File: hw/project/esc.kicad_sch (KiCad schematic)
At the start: 0 parts

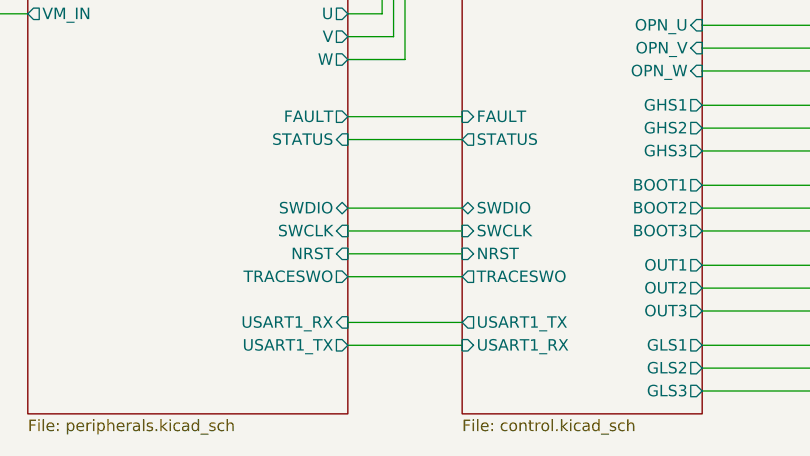
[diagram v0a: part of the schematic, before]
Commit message: Revise hall sensor inputs
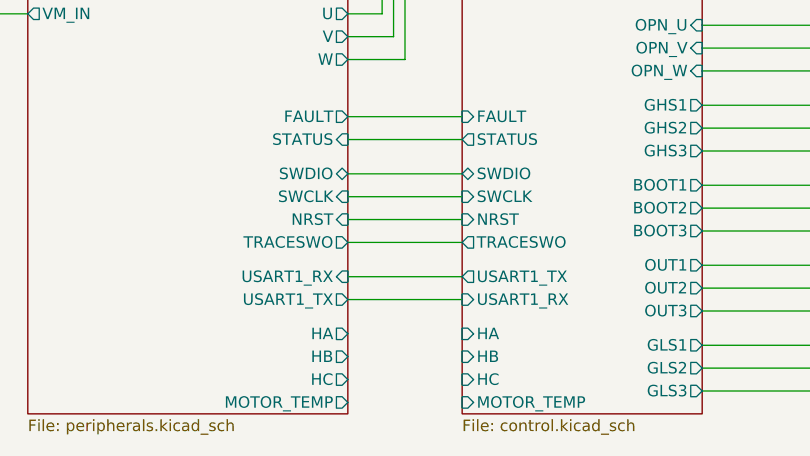
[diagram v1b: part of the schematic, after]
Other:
- sheet Control ports: added HA, HB, HC, MOTOR_TEMP; removed none
- sheet Peripherals ports: added HA, HB, HC, MOTOR_TEMP; removed none
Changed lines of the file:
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@@
 	(wire
 		(pts
-			(xy 165.1 123.19) (xy 152.4 123.19)
-		)
-		(stroke
-			(width 0)
-			(type default)
-		)
-	)
-	(wire
-		(pts
-			(xy 165.1 113.03) (xy 152.4 113.03)
+			(xy 165.1 118.11) (xy 152.4 118.11)
+		)
+		(stroke
+			(width 0)
+			(type default)
+		)
+	)
+	(wire
+		(pts
+			(xy 165.1 109.22) (xy 152.4 109.22)
 		)
 		(stroke
@@
 	(wire
 		(pts
-			(xy 165.1 107.95) (xy 152.4 107.95)
+			(xy 165.1 104.14) (xy 152.4 104.14)
 		)
 		(stroke
@@
 	(wire
 		(pts
-			(xy 165.1 120.65) (xy 152.4 120.65)
+			(xy 165.1 115.57) (xy 152.4 115.57)
 		)
 		(stroke
@@
 	(wire
 		(pts
-			(xy 165.1 110.49) (xy 152.4 110.49)
+			(xy 165.1 106.68) (xy 152.4 106.68)
 		)
 		(stroke
@@
 	(wire
 		(pts
-			(xy 165.1 115.57) (xy 152.4 115.57)
+			(xy 165.1 111.76) (xy 152.4 111.76)
 		)
 		(stroke
@@
 		)
 		(pin "NRST" input
-			(at 165.1 113.03 180)
+			(at 165.1 109.22 180)
 			(effects
 				(font
@@
 		)
 		(pin "SWCLK" input
-			(at 165.1 110.49 180)
+			(at 165.1 106.68 180)
 			(effects
 				(font
@@
 		)
 		(pin "TRACESWO" output
-			(at 165.1 115.57 180)
+			(at 165.1 111.76 180)
 			(effects
 				(font
@@
 		)
 		(pin "SWDIO" bidirectional
-			(at 165.1 107.95 180)
+			(at 165.1 104.14 180)
 			(effects
 				(font
@@
 		)
 		(pin "USART1_TX" output
-			(at 165.1 120.65 180)
+			(at 165.1 115.57 180)
 			(effects
 				(font
@@
 		)
 		(pin "USART1_RX" input
-			(at 165.1 123.19 180)
+			(at 165.1 118.11 180)
 			(effects
 				(font
@@
 		(pin "STATUS" output
 			(at 165.1 100.33 180)
+			(effects
+				(font
+					(size 1.27 1.27)
+				)
+				(justify left)
+			)
+		)
+		(pin "HA" input
+			(at 165.1 121.92 180)
+			(effects
+				(font
+					(size 1.27 1.27)
+				)
+				(justify left)
+			)
+		)
+		(pin "HB" input
+			(at 165.1 124.46 180)
+			(effects
+				(font
+					(size 1.27 1.27)
+				)
+				(justify left)
+			)
+		)
+		(pin "HC" input
+			(at 165.1 127 180)
+			(effects
+				(font
+					(size 1.27 1.27)
+				)
+				(justify left)
+			)
+		)
+		(pin "MOTOR_TEMP" input
+			(at 165.1 129.54 180)
 			(effects
 				(font
@@
 		)
 		(pin "NRST" input
-			(at 152.4 113.03 0)
+			(at 152.4 109.22 0)
 			(effects
 				(font
@@
 		)
 		(pin "SWCLK" input
-			(at 152.4 110.49 0)
+			(at 152.4 106.68 0)
 			(effects
 				(font
@@
 		)
 		(pin "SWDIO" bidirectional
-			(at 152.4 107.95 0)
+			(at 152.4 104.14 0)
 			(effects
 				(font
@@
 		)
 		(pin "TRACESWO" output
-			(at 152.4 115.57 0)
+			(at 152.4 111.76 0)
 			(effects
 				(font
@@
 		)
 		(pin "USART1_RX" input
-			(at 152.4 120.65 0)
+			(at 152.4 115.57 0)
 			(effects
 				(font
@@
 		)
 		(pin "USART1_TX" output
-			(at 152.4 123.19 0)
+			(at 152.4 118.11 0)
 			(effects
 				(font
@@
 			)
 		)
+		(pin "HA" output
+			(at 152.4 121.92 0)
+			(effects
+				(font
+					(size 1.27 1.27)
+				)
+				(justify right)
+			)
+		)
+		(pin "HB" output
+			(at 152.4 124.46 0)
+			(effects
+				(font
+					(size 1.27 1.27)
+				)
+				(justify right)
+			)
+		)
+		(pin "HC" output
+			(at 152.4 127 0)
+			(effects
+				(font
+					(size 1.27 1.27)
+				)
+				(justify right)
+			)
+		)
+		(pin "MOTOR_TEMP" output
+			(at 152.4 129.54 0)
+			(effects
+				(font
+					(size 1.27 1.27)
+				)
+				(justify right)
+			)
+		)

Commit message: can tranceiver
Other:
- sheet Control ports: added CAN_STBY, FDCAN1_RX, FDCAN1_TX; removed none
- sheet Peripherals ports: added RXD, STBY, TXD; removed none
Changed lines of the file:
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@@
+	(wire
+		(pts
+			(xy 152.4 140.97) (xy 165.1 140.97)
+		)
+		(stroke
+			(width 0)
+			(type default)
+		)
+	)
 	(wire
 		(pts
@@
 	(wire
 		(pts
+			(xy 152.4 146.05) (xy 165.1 146.05)
+		)
+		(stroke
+			(width 0)
+			(type default)
+		)
+	)
+	(wire
+		(pts
 			(xy 157.48 88.9) (xy 152.4 88.9)
 		)
@@
 		(pts
 			(xy 156.21 69.85) (xy 156.21 86.36)
+		)
+		(stroke
+			(width 0)
+			(type default)
+		)
+	)
+	(wire
+		(pts
+			(xy 152.4 143.51) (xy 165.1 143.51)
 		)
 		(stroke
@@
 	(sheet
 		(at 165.1 80.01)
-		(size 26.67 50.8)
+		(size 26.67 80.01)
 		(exclude_from_sim no)
 		(in_bom yes)
@@
 		)
 		(property "Sheetfile" "control.kicad_sch"
-			(at 165.1 131.3946 0)
+			(at 165.1 160.6046 0)
 			(show_name no)
 			(do_not_autoplace no)
@@
 		(pin "MOTOR_TEMP" input
 			(at 165.1 129.54 180)
+			(effects
+				(font
+					(size 1.27 1.27)
+				)
+				(justify left)
+			)
+		)
+		(pin "FDCAN1_TX" output
+			(at 165.1 140.97 180)
+			(effects
+				(font
+					(size 1.27 1.27)
+				)
+				(justify left)
+			)
+		)
+		(pin "FDCAN1_RX" input
+			(at 165.1 143.51 180)
+			(effects
+				(font
+					(size 1.27 1.27)
+				)
+				(justify left)
+			)
+		)
+		(pin "CAN_STBY" output
+			(at 165.1 146.05 180)
 			(effects
 				(font
@@
 	(sheet
 		(at 116.84 80.01)
-		(size 35.56 50.8)
+		(size 35.56 80.01)
 		(exclude_from_sim no)
 		(in_bom yes)
@@
 		)
 		(property "Sheetfile" "peripherals.kicad_sch"
-			(at 116.84 131.3946 0)
+			(at 116.84 160.6046 0)
 			(show_name no)
 			(do_not_autoplace no)
@@
 		(pin "MOTOR_TEMP" output
 			(at 152.4 129.54 0)
+			(effects
+				(font
+					(size 1.27 1.27)
+				)
+				(justify right)
+			)
+		)
+		(pin "RXD" input
+			(at 152.4 143.51 0)
+			(effects
+				(font
+					(size 1.27 1.27)
+				)
+				(justify right)
+			)
+		)
+		(pin "STBY" input
+			(at 152.4 146.05 0)
+			(effects
+				(font
+					(size 1.27 1.27)
+				)
+				(justify right)
+			)
+		)
+		(pin "TXD" input
+			(at 152.4 140.97 0)
 			(effects
 				(font
@@
 	(sheet
 		(at 208.28 80.01)
-		(size 40.64 50.8)
+		(size 40.64 54.61)
 		(exclude_from_sim no)
 		(in_bom yes)
@@
 		)
 		(property "Sheetfile" "drive.kicad_sch"
-			(at 208.28 131.3946 0)
+			(at 208.28 135.2046 0)
 			(show_name no)
 			(do_not_autoplace no)

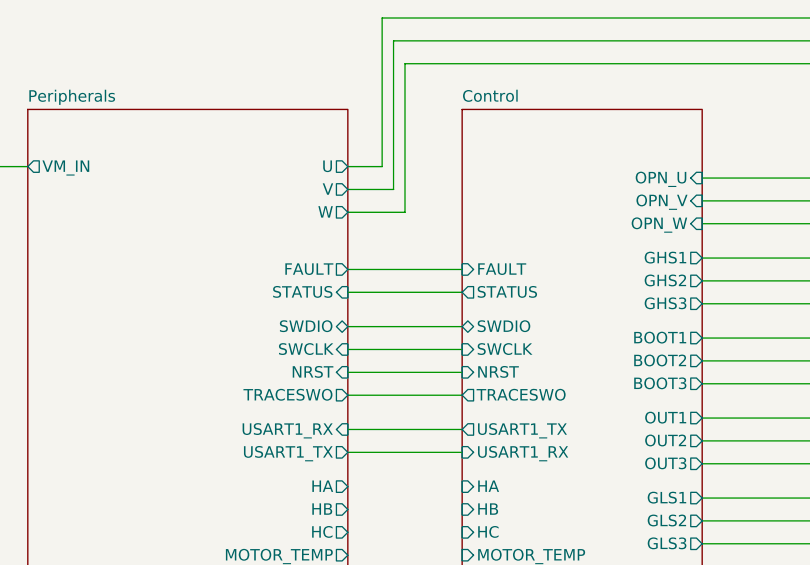
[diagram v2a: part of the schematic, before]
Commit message: Checkpoint for setting up user command inputs
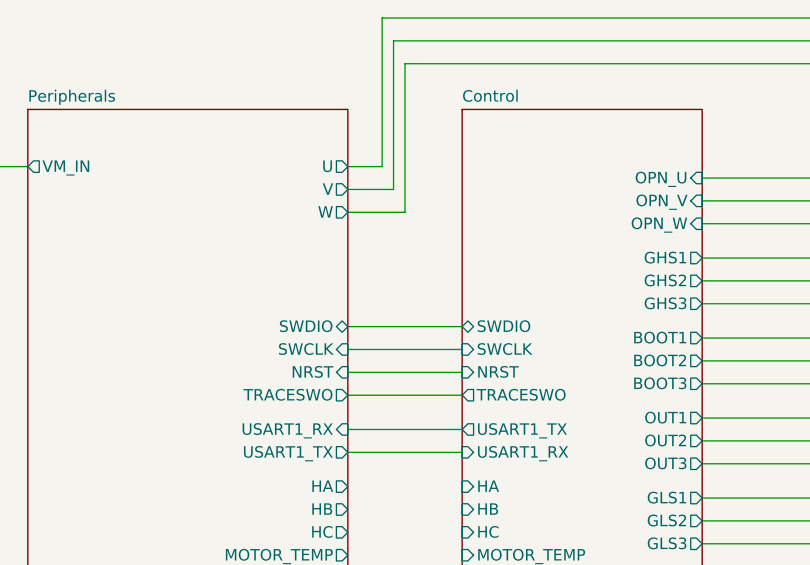
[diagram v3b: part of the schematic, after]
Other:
- sheet Control ports: added none; removed FAULT, STATUS
- sheet Peripherals ports: added none; removed FAULT, STATUS
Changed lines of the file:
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@@
-	(wire
-		(pts
-			(xy 165.1 97.79) (xy 152.4 97.79)
-		)
-		(stroke
-			(width 0)
-			(type default)
-		)
-	)
 	(wire
 		(pts
@@
 		(pts
 			(xy 208.28 90.17) (xy 191.77 90.17)
-		)
-		(stroke
-			(width 0)
-			(type default)
-		)
-	)
-	(wire
-		(pts
-			(xy 165.1 100.33) (xy 152.4 100.33)
 		)
 		(stroke
@@
 			)
 		)
-		(pin "FAULT" input
-			(at 165.1 97.79 180)
-			(effects
-				(font
-					(size 1.27 1.27)
-				)
-				(justify left)
-			)
-		)
-		(pin "STATUS" output
-			(at 165.1 100.33 180)
-			(effects
-				(font
-					(size 1.27 1.27)
-				)
-				(justify left)
-			)
-		)
 		(pin "HA" input
 			(at 165.1 121.92 180)
@@
 			(effects
 				(font
-					(size 1.27 1.27)
-				)
-				(justify right)
-			)
-		)
-		(pin "FAULT" output
-			(at 152.4 97.79 0)
-			(effects
-				(font
-					(size 1.27 1.27)
-				)
-				(justify right)
-			)
-		)
-		(pin "STATUS" input
-			(at 152.4 100.33 0)
-			(effects
-				(font

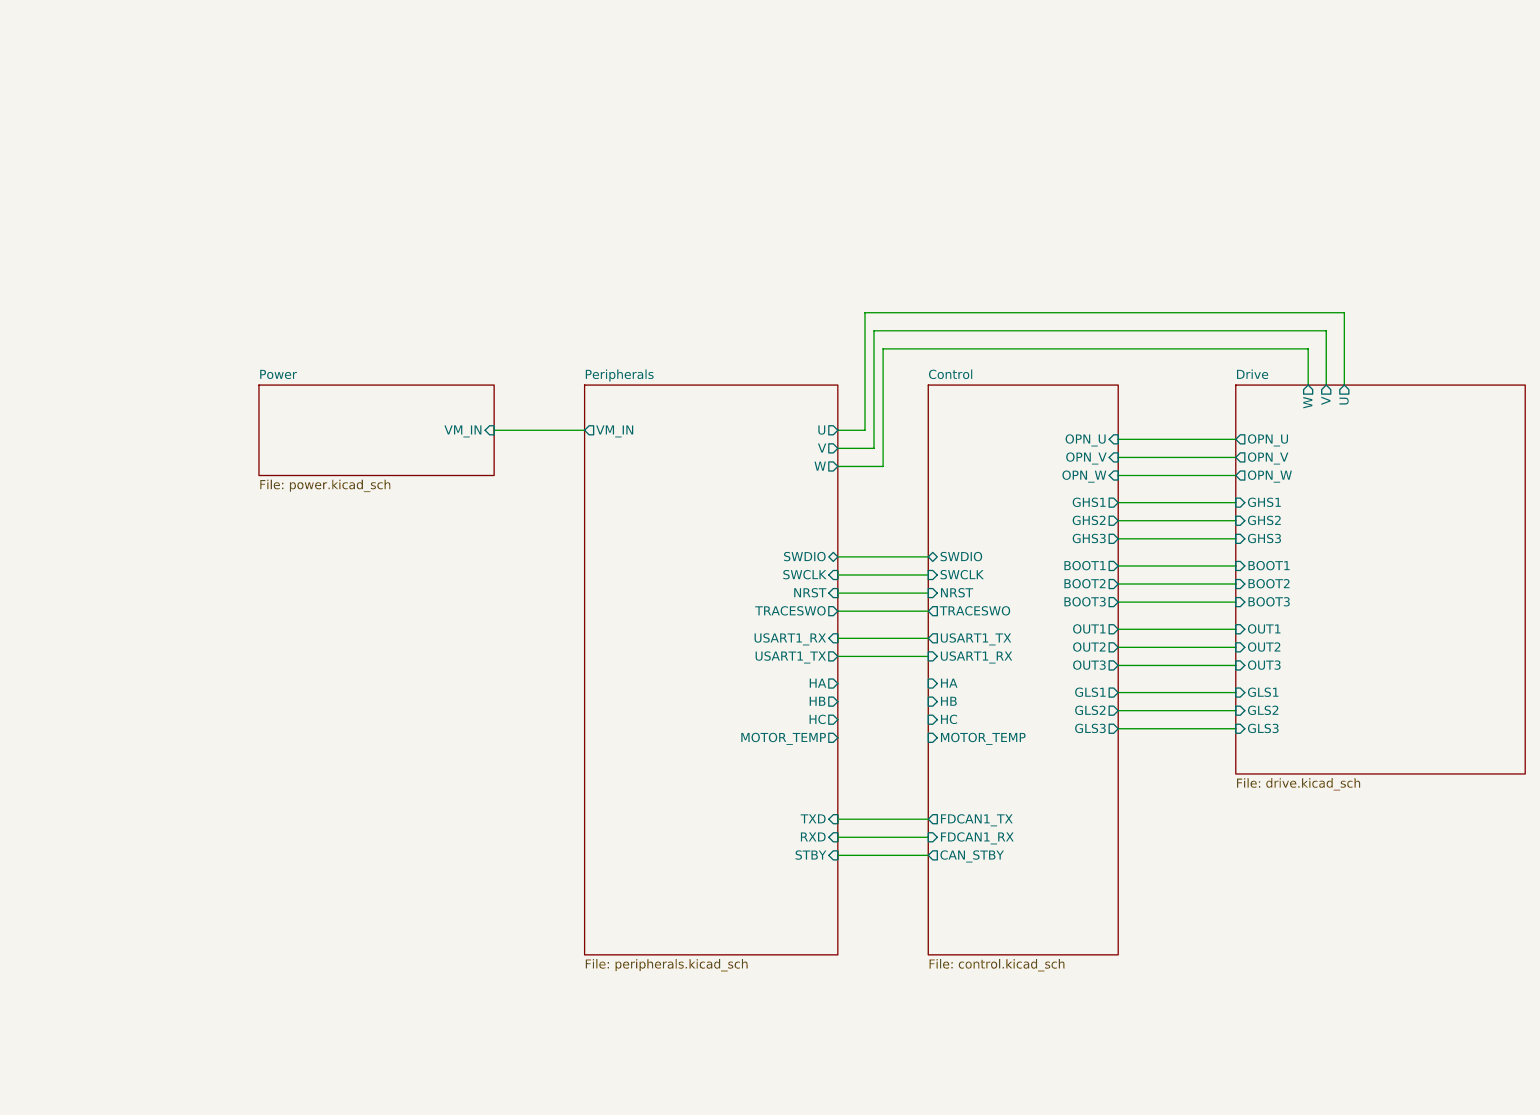
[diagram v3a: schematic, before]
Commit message: Wire up specific signals
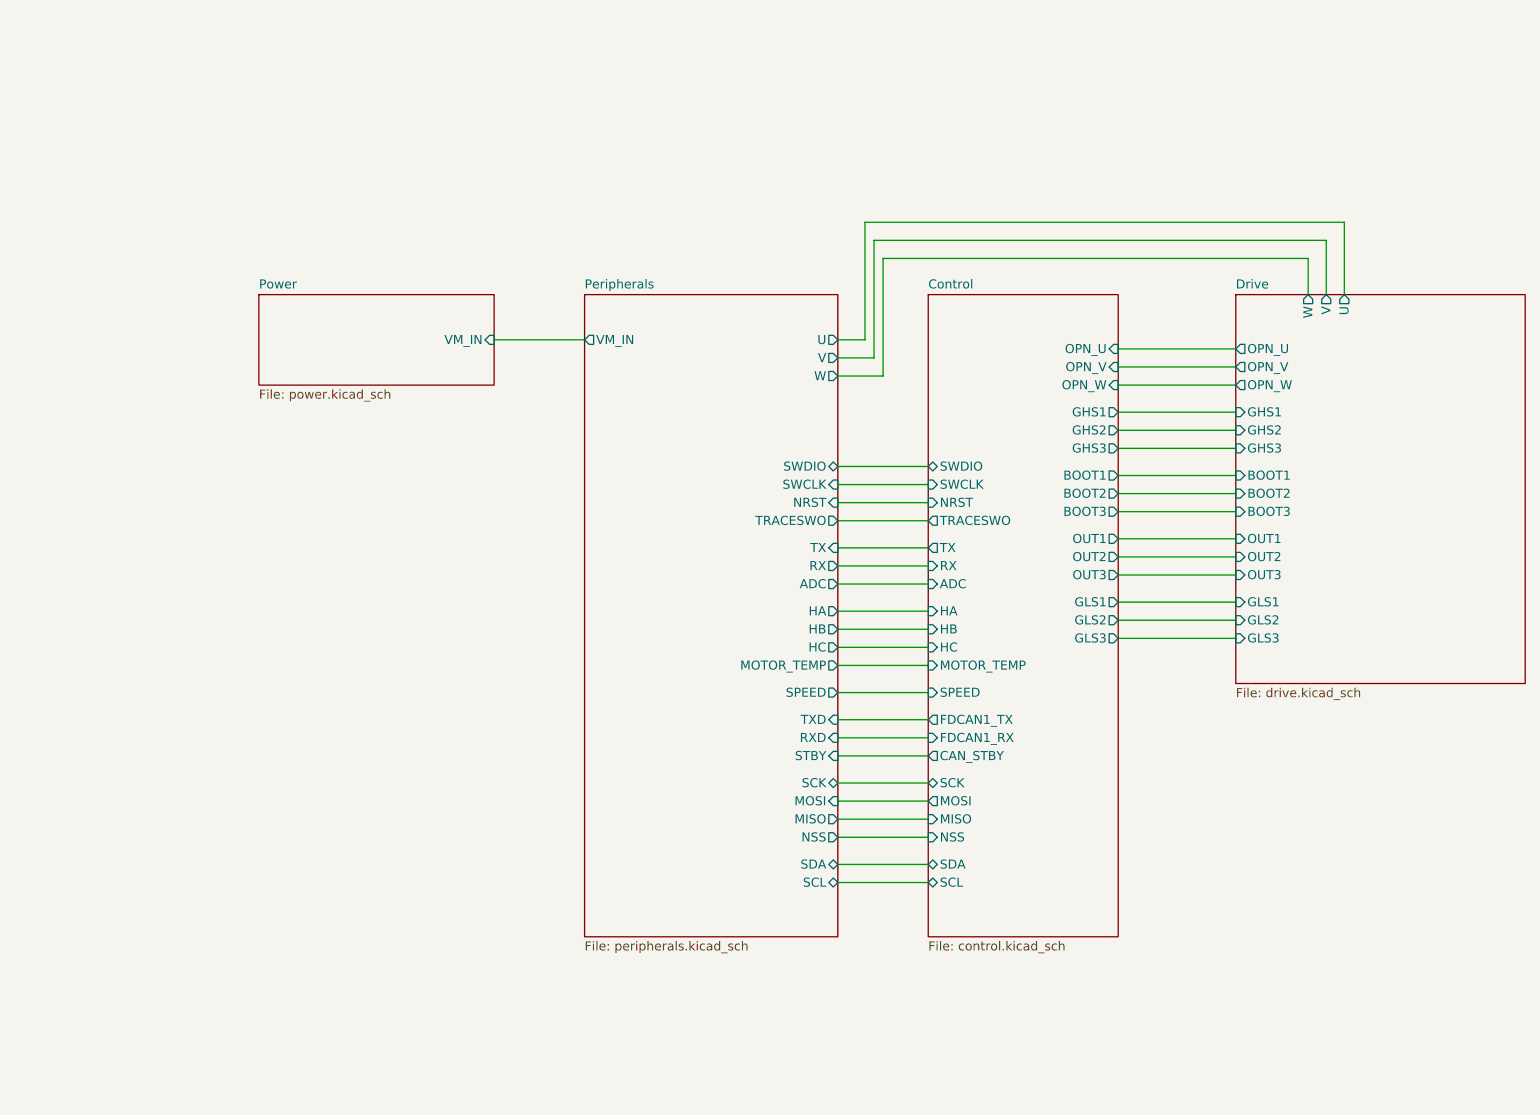
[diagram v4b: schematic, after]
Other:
- sheet Control ports: added ADC, MISO, MOSI, NSS, RX, SCK, SCL, SDA, SPEED, TX; removed USART1_RX, USART1_TX
- sheet Peripherals ports: added ADC, MISO, MOSI, NSS, RX, SCK, SCL, SDA, SPEED, TX; removed USART1_RX, USART1_TX
